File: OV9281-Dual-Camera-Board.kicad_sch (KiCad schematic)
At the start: 83 parts, among them J3 Conn_FFC_WE_68715014522_TWO-S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, Q1 BSS138AKA, U1 ImageSensor_OV9281, U2 ImageSensor_OV9281, U3 NTS0104BQ, U4 NTB0104BQ, U5 TLV73318PDBVT, U6 TLV73312PDBVT, U7 TLV73328PDBVT, Y1 7C-24.000MBB-T, Y2 7C-24.000MBB-T

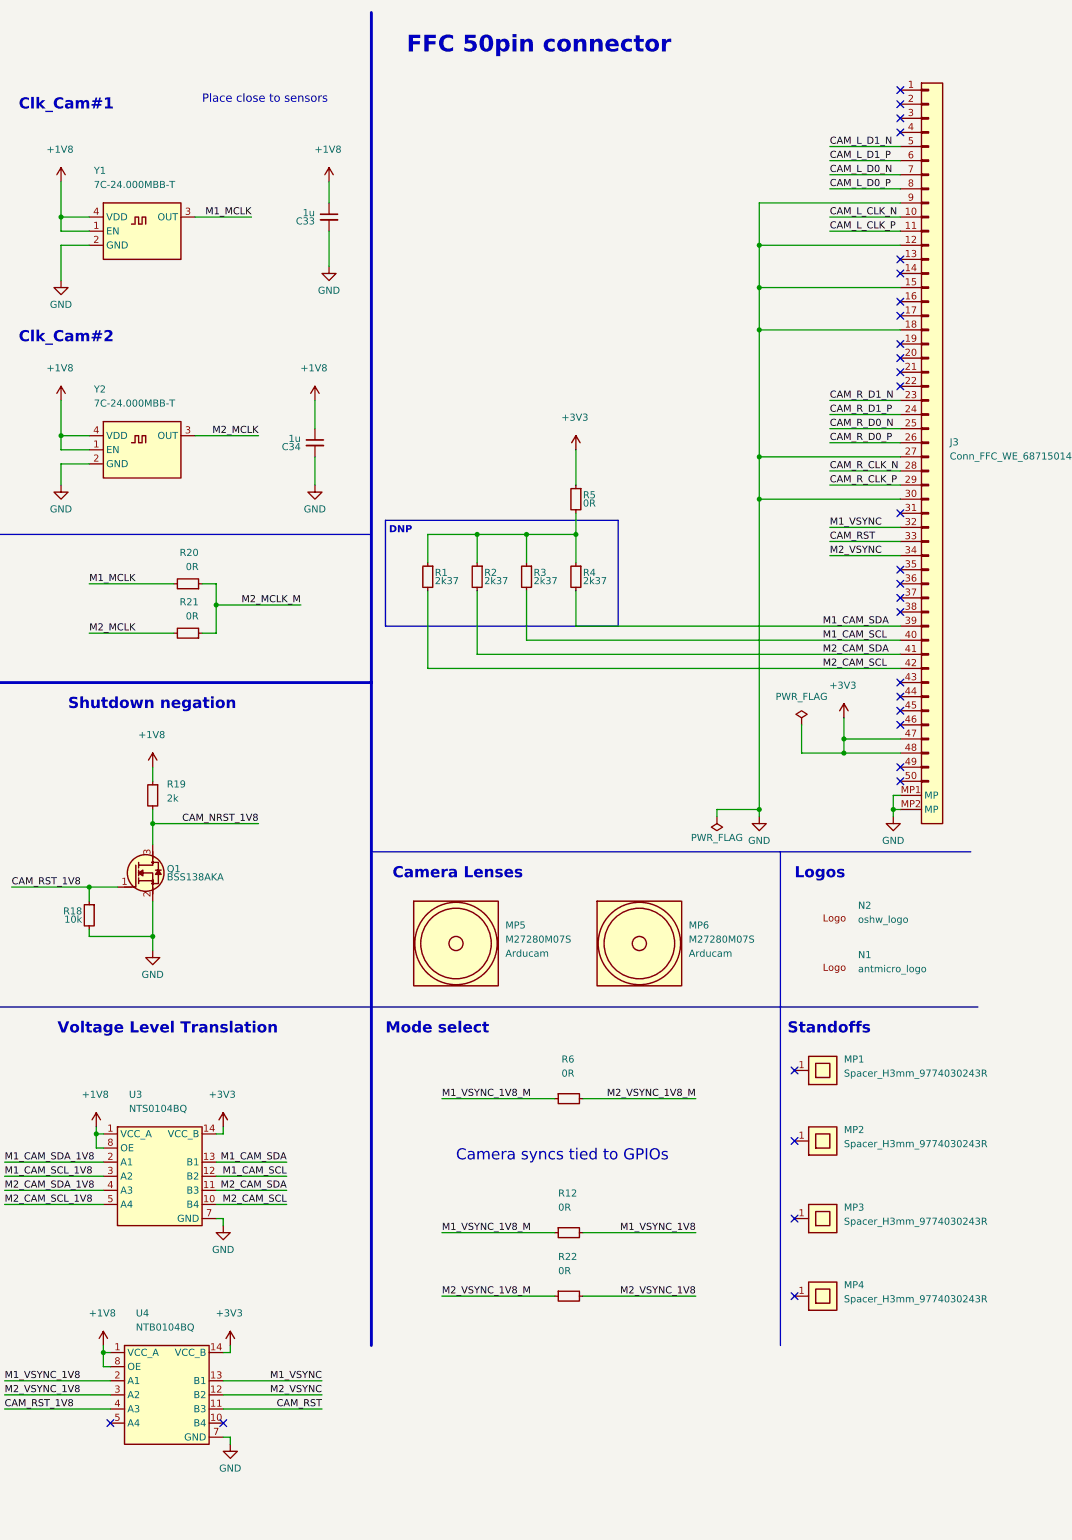
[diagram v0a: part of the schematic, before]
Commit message: [#49221] Update symbols and add fiducials
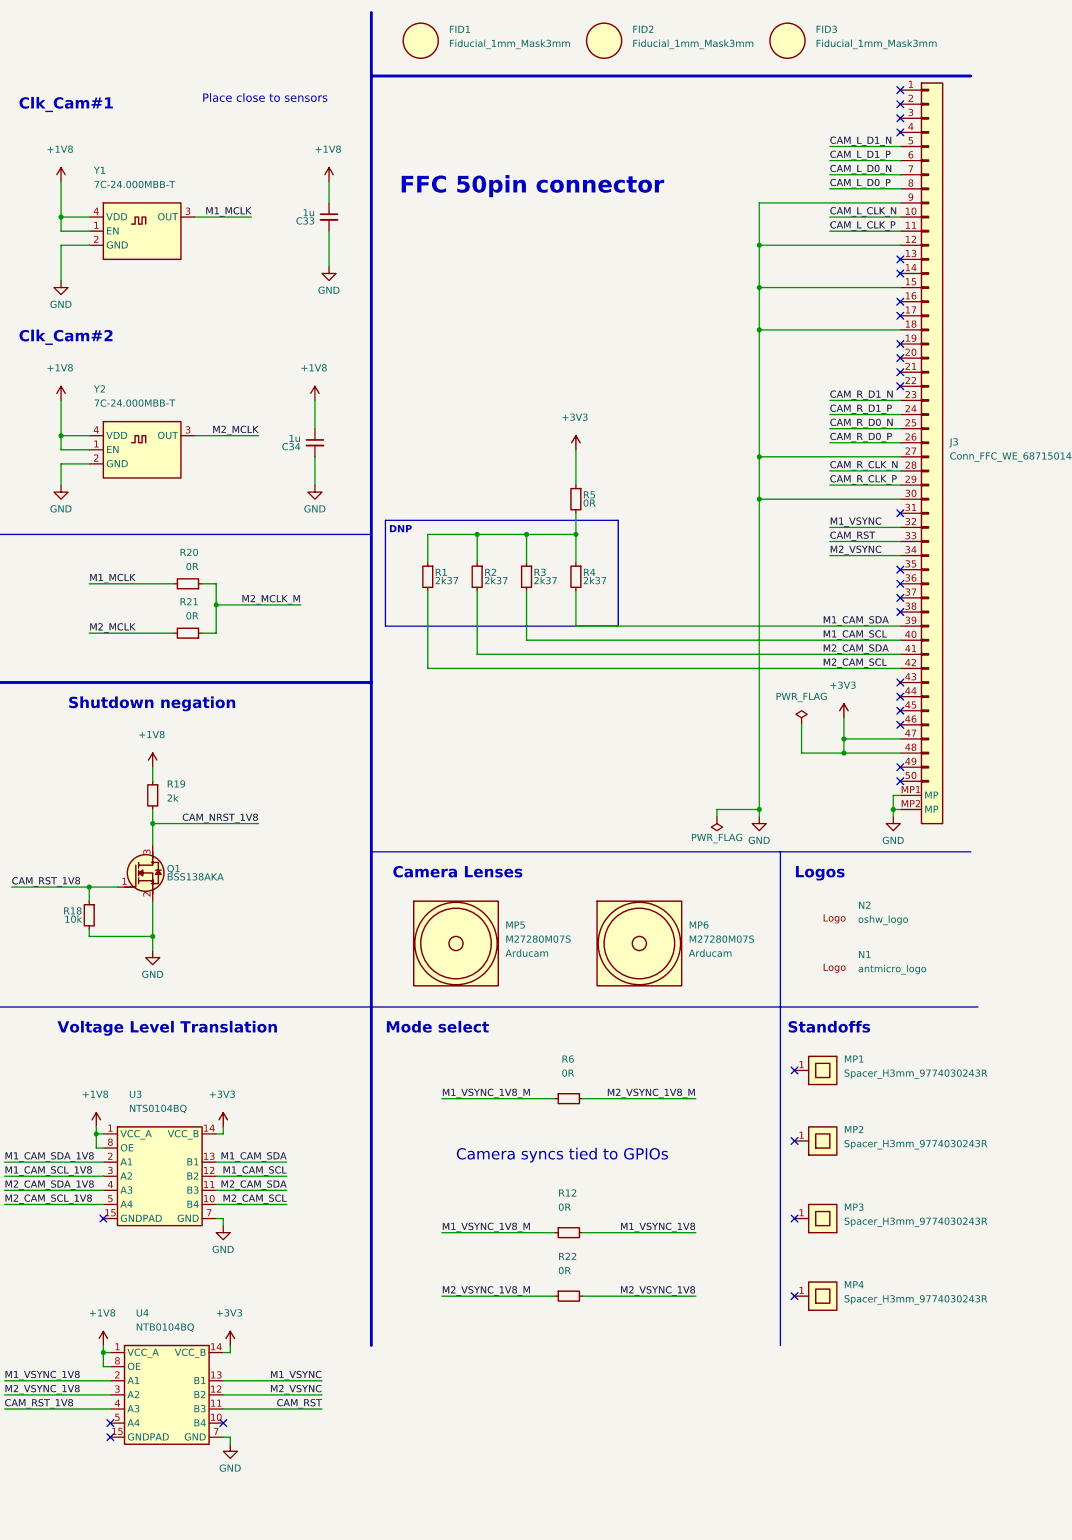
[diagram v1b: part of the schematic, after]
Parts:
- added FID1, FID2, FID3: Fiducial_1mm_Mask3mm, antmicro-footprints:Fiducial_1mm_Mask3mm, symbol antmicroFiducialMarks:Fiducial_1mm_Mask3mm
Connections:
- no-connect marks 51 -> 53

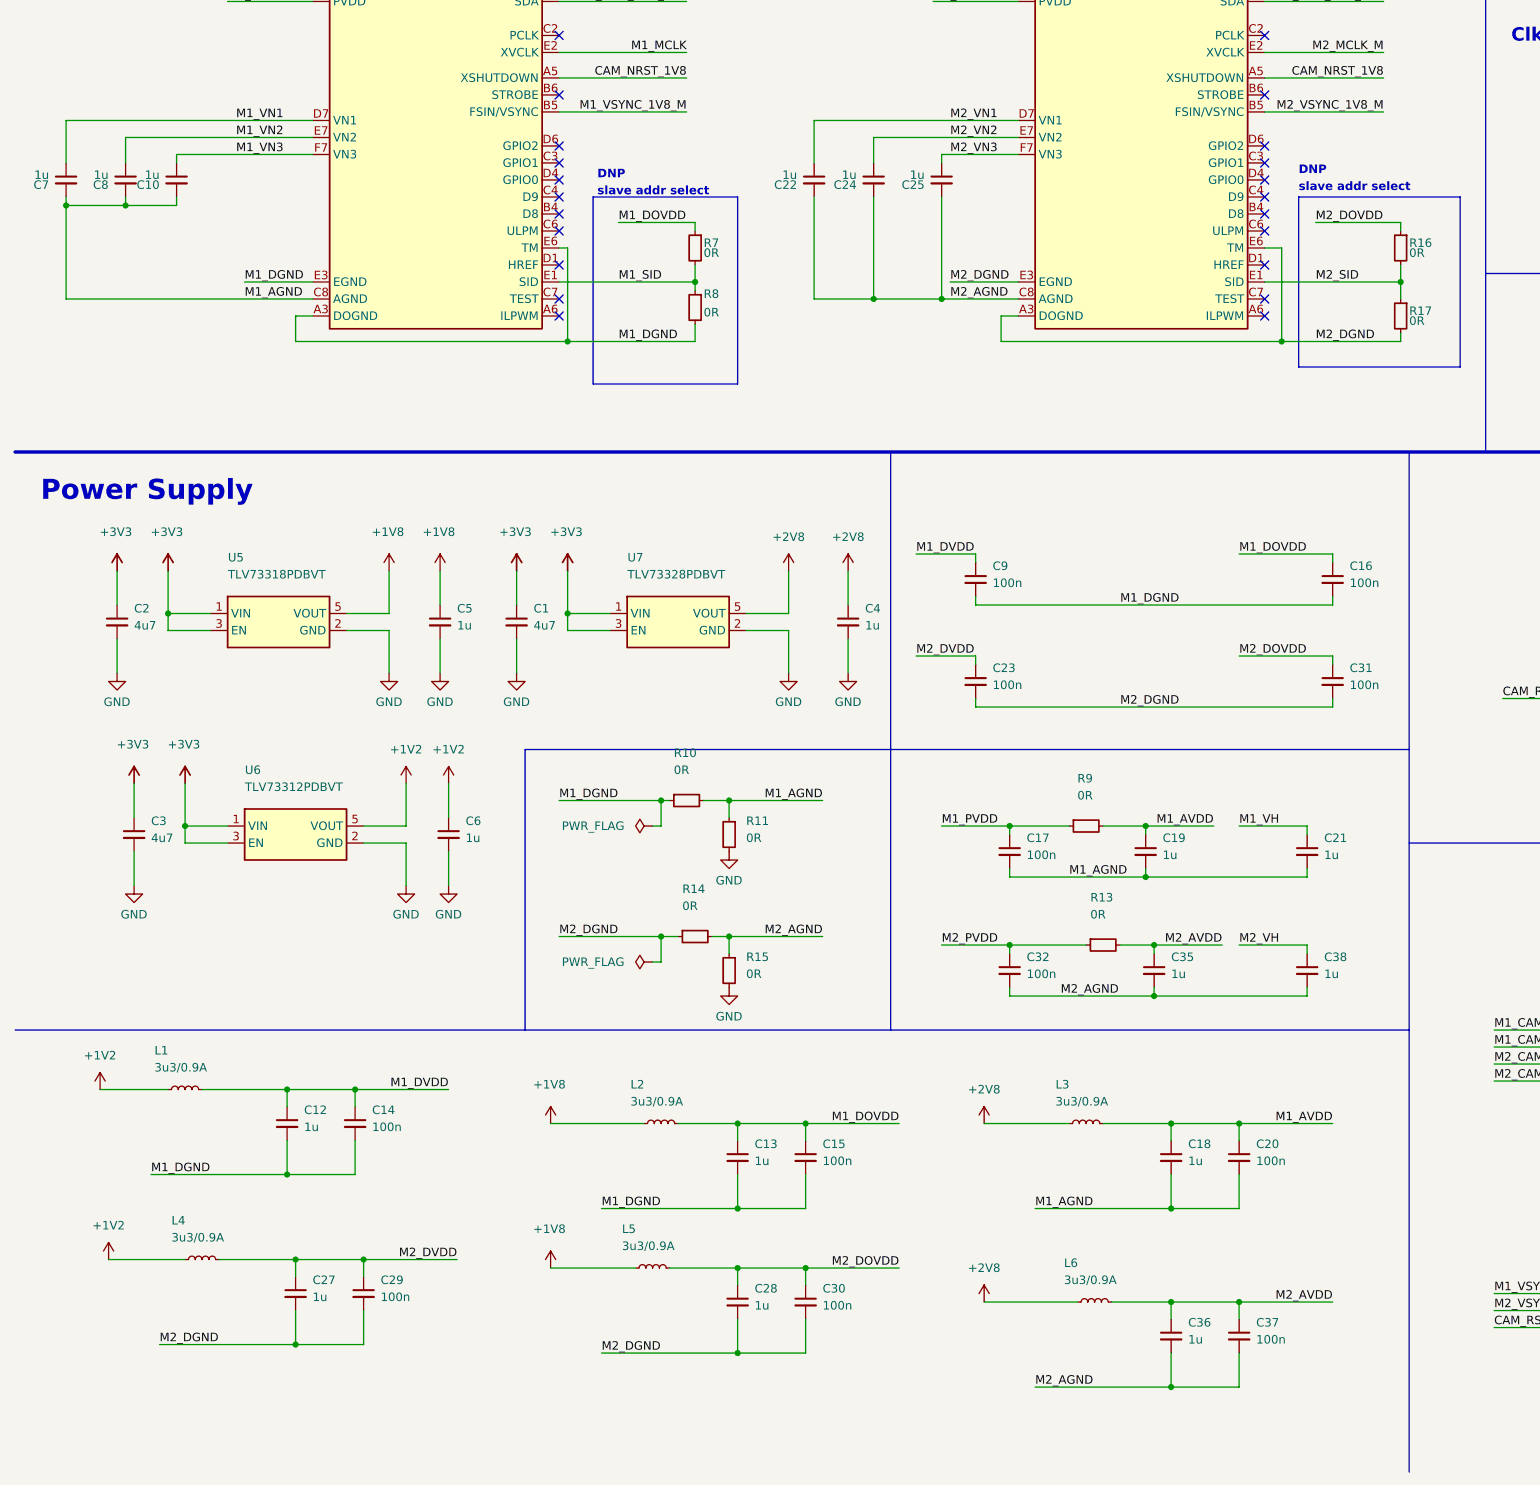
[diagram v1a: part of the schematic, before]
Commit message: Improved layout for signal integrity [#50177]
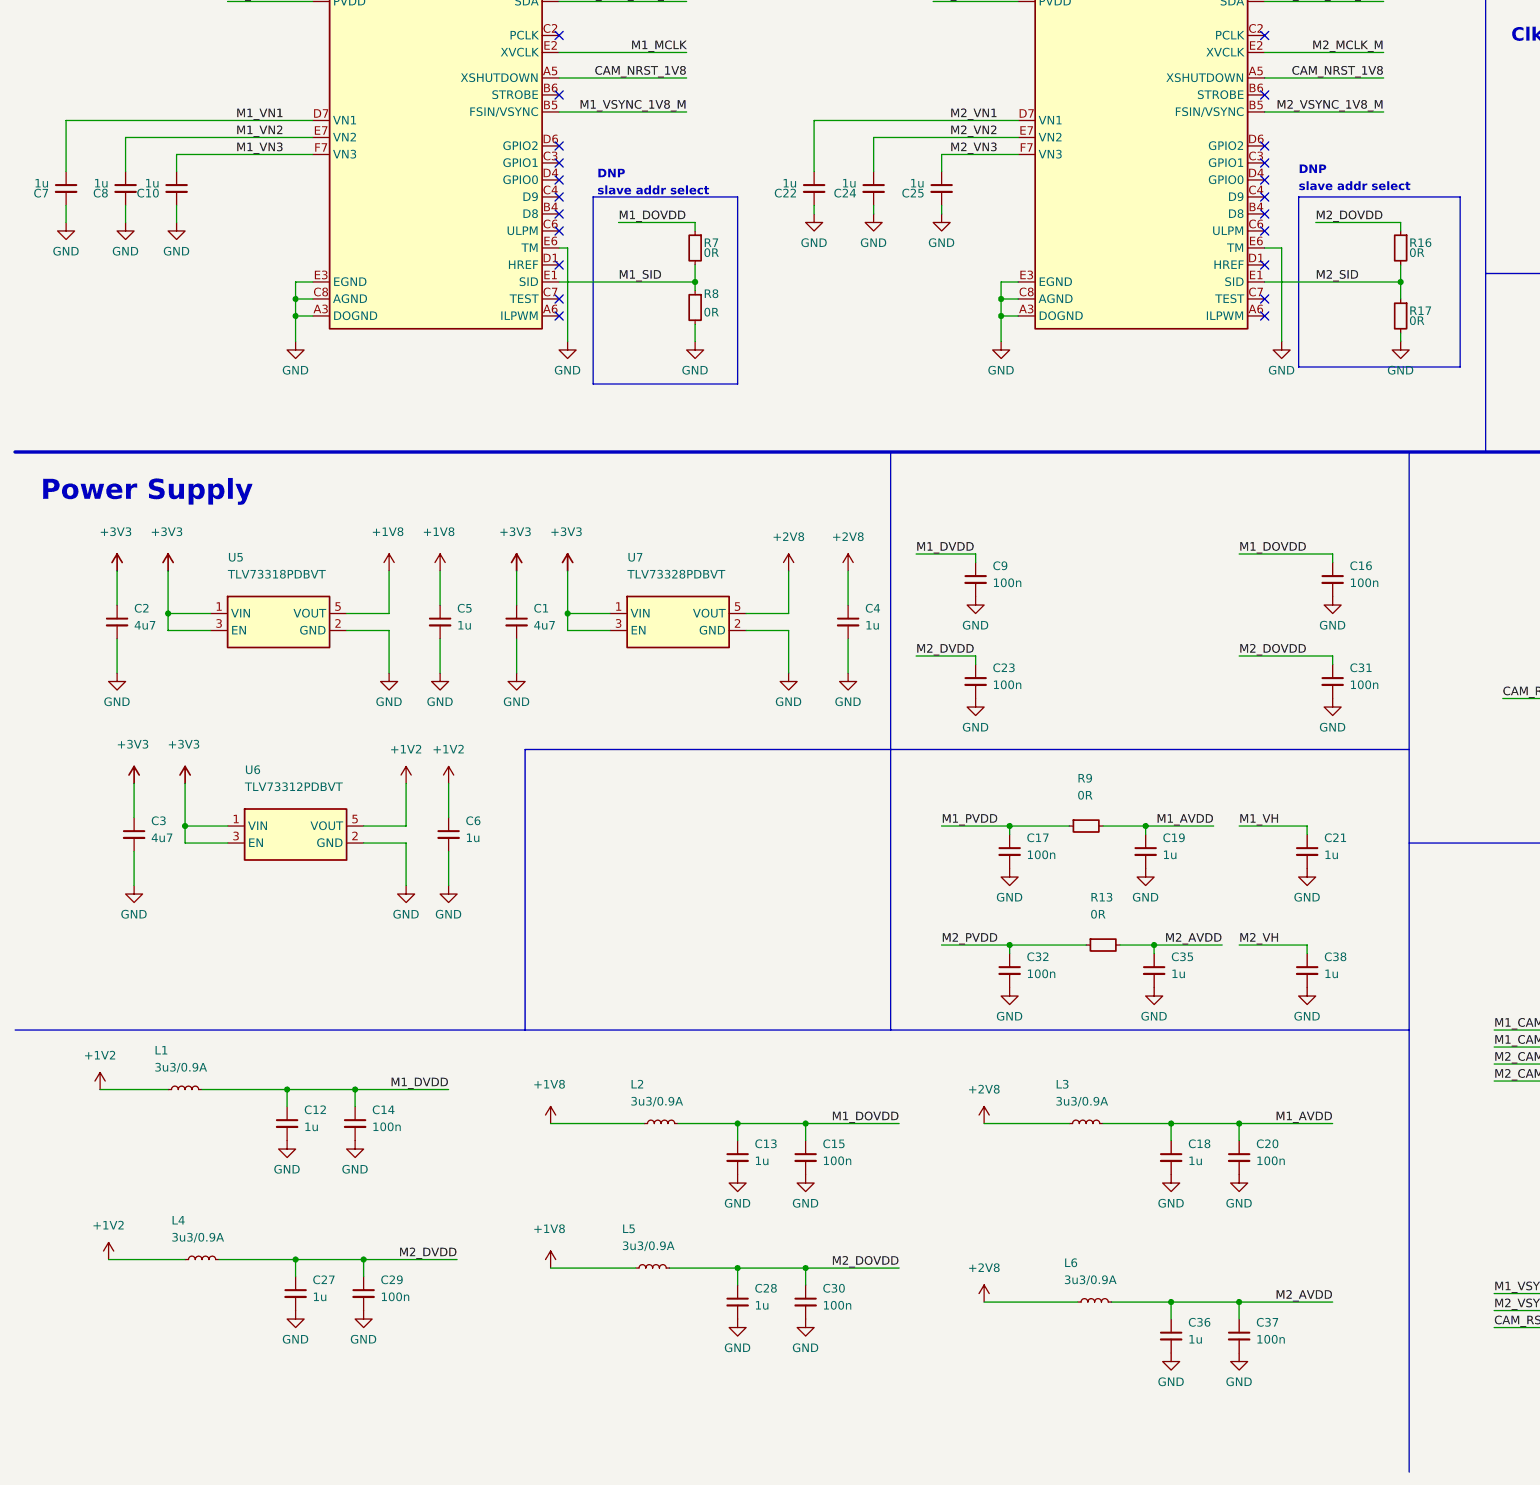
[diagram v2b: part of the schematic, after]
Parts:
- removed R10, R11, R14, R15: R_0R_0402, antmicro-footprints:R_0402_1005Metric, symbol antmicroResistors0402:R_0R_0402
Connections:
- net M1_AGND is gone; now on net GND: C10.2, C17.2, C18.2, C19.2, C20.2, C21.2, C7.2, C8.2, U1.C8 (AGND), U1.D2 (AGND), U1.F8 (AGND), U1.H7 (AGND)
- net M1_DGND is gone; now on net GND: C12.2, C13.2, C14.2, C15.2, C16.2, C9.2, R8.2, U1.A3 (DOGND), U1.A7 (DOGND), U1.B2 (DOGND), U1.E3 (EGND), U1.E5 (EGND), U1.E6 (TM), U1.F1 (DOGND), U1.F4 (DOGND), U1.F6 (DOGND), U1.G2 (DOGND)
- net M2_AGND is gone; now on net GND: C22.2, C24.2, C25.2, C32.2, C35.2, C36.2, C37.2, C38.2, U2.C8 (AGND), U2.D2 (AGND), U2.F8 (AGND), U2.H7 (AGND)
- net M2_DGND is gone; now on net GND: C23.2, C27.2, C28.2, C29.2, C30.2, C31.2, R17.2, U2.A3 (DOGND), U2.A7 (DOGND), U2.B2 (DOGND), U2.E3 (EGND), U2.E5 (EGND), U2.E6 (TM), U2.F1 (DOGND), U2.F4 (DOGND), U2.F6 (DOGND), U2.G2 (DOGND)
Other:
- moved on the sheet: C10, C22, C24, C25, C7, C8
